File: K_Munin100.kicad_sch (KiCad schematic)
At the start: 95 parts, among them IC2 ACHS-7123-000E, J1 Conn_Coaxial, J19 To P.A., J2 Conn_Coaxial, J3 Conn_02x03_Odd_Even, J5 Wurth Redcube 7461057, J6 Phoenix/1711725, J7 Wurth Redcube 7461057, Q1 MRF101AN tab dwn, Q2 MRF 101BN tab up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

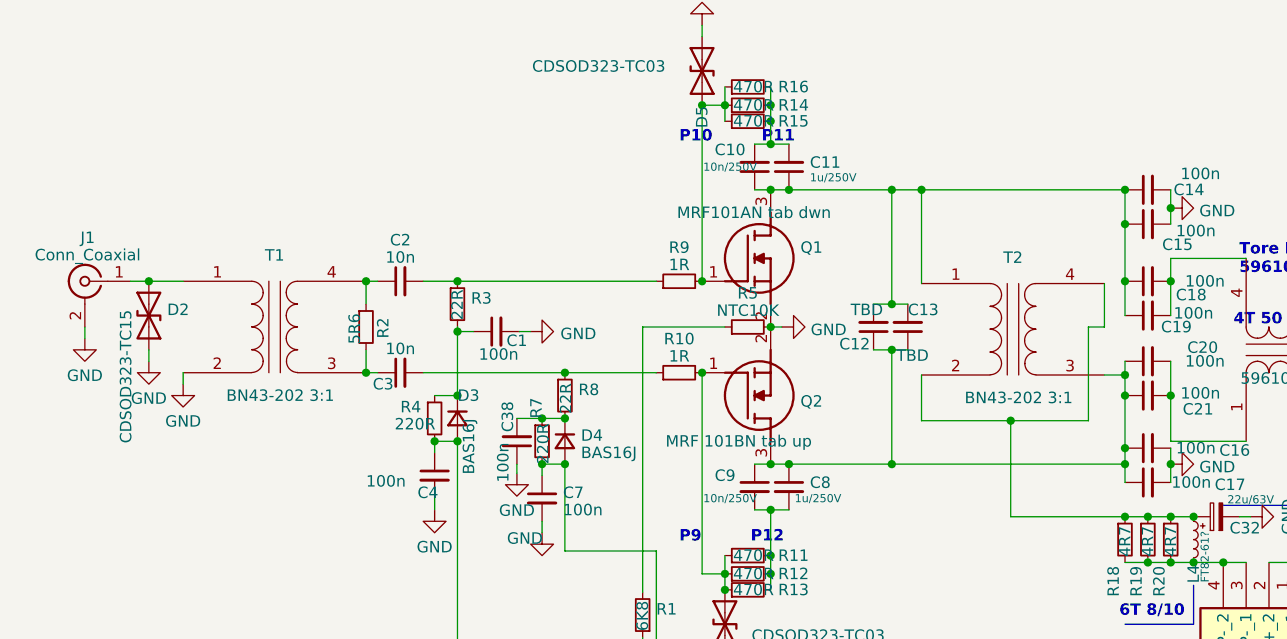
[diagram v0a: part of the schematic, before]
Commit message: Munin 400 mod with MRF101 AN/BN
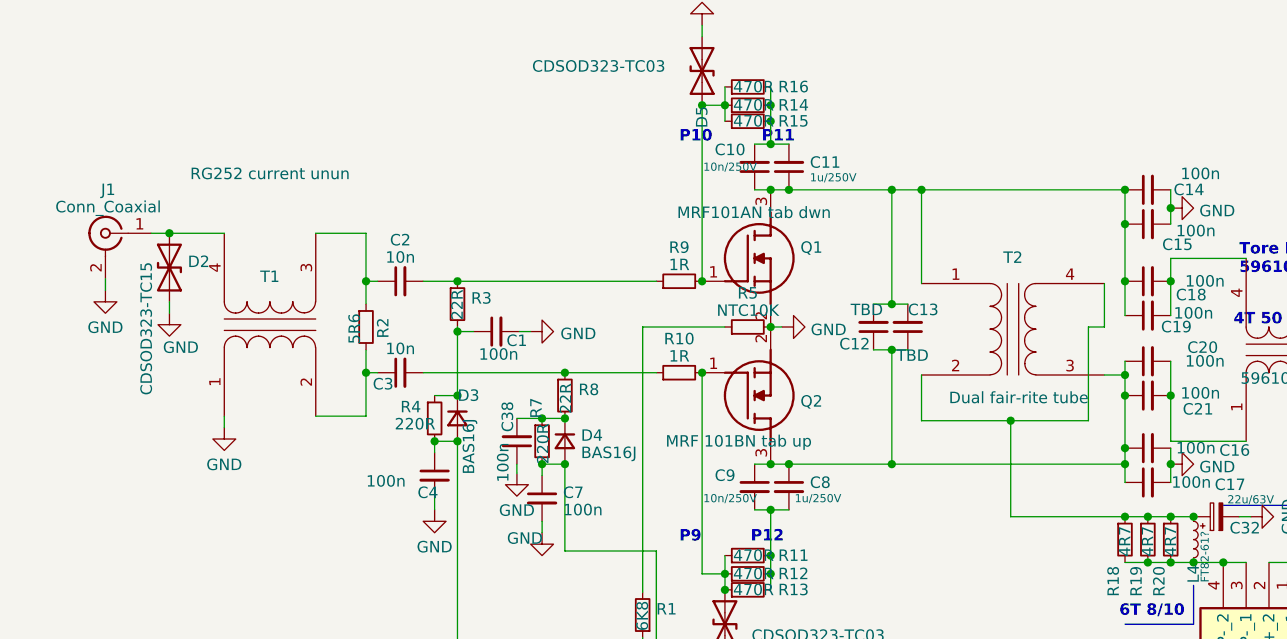
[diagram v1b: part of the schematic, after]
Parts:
- T1: value BN43-202 3:1 -> RG252 current unun
- T2: value BN43-202 3:1 -> Dual fair-rite tube
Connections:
- net GND: now also T1.1 (AA); no longer T1.2 (AB)
- net at D2.2 (A2), J1.1 (In): now also T1.4 (SB); no longer T1.1 (AA)
- net at C2.1, R2.1: now also T1.3 (SA); no longer T1.4 (SB)
- net at C3.1, R2.2: now also T1.2 (AB); no longer T1.3 (SA)
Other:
- moved on the sheet: D2, J1, T1
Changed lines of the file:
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@@
 	)
 	(junction
+		(at 64.008 56.134)
+		(diameter 0)
+		(color 0 0 0 0)
+	)
+	(junction
 		(at 108.966 76.454)
 		(diameter 0)
@@
 	)
 	(junction
-		(at 64.008 56.134)
-		(diameter 0)
-		(color 0 0 0 0)
-	)
-	(junction
 		(at 88.138 133.604)
 		(diameter 0)
@@
 	)
 	(junction
+		(at 64.008 45.974)
+		(diameter 0)
+		(color 0 0 0 0)
+	)
+	(junction
 		(at 86.106 56.134)
 		(diameter 0)
@@
 	)
 	(junction
-		(at 39.878 45.974)
+		(at 42.164 40.64)
 		(diameter 0)
 		(color 0 0 0 0)
@@
 	)
 	(junction
-		(at 64.008 45.974)
-		(diameter 0)
-		(color 0 0 0 0)
-	)
-	(junction
 		(at 148.336 58.674)
 		(diameter 0)
@@
 	(wire
 		(pts
+			(xy 58.42 60.96) (xy 64.008 60.96)
+		)
+		(stroke
+			(width 0)
+			(type default)
+		)
+	)
+	(wire
+		(pts
 			(xy 81.026 51.562) (xy 82.296 51.562)
 		)
@@
 	(wire
 		(pts
-			(xy 39.878 53.594) (xy 39.878 54.864)
+			(xy 42.164 48.26) (xy 42.164 49.53)
 		)
 		(stroke
@@
 	(wire
 		(pts
+			(xy 64.008 45.974) (xy 64.008 40.64)
+		)
+		(stroke
+			(width 0)
+			(type default)
+		)
+	)
+	(wire
+		(pts
 			(xy 122.428 66.294) (xy 148.336 66.294)
 		)
@@
 	(wire
 		(pts
-			(xy 39.878 45.974) (xy 43.688 45.974)
+			(xy 42.164 40.64) (xy 48.26 40.64)
 		)
 		(stroke
@@
 	(wire
 		(pts
-			(xy 37.846 45.974) (xy 39.878 45.974)
+			(xy 40.132 40.64) (xy 42.164 40.64)
 		)
 		(stroke
@@
 	(wire
 		(pts
+			(xy 64.008 40.64) (xy 58.42 40.64)
+		)
+		(stroke
+			(width 0)
+			(type default)
+		)
+	)
+	(wire
+		(pts
 			(xy 101.346 121.666) (xy 101.346 122.936)
 		)
@@
 	(wire
 		(pts
-			(xy 43.688 56.134) (xy 43.688 57.404)
+			(xy 48.26 60.96) (xy 48.26 62.23)
 		)
 		(stroke
@@
 	(wire
 		(pts
+			(xy 64.008 60.96) (xy 64.008 56.134)
+		)
+		(stroke
+			(width 0)
+			(type default)
+		)
+	)
+	(wire
+		(pts
 			(xy 165.608 136.906) (xy 165.608 133.096)
 		)
@@
 	(wire
 		(pts
-			(xy 32.766 51.054) (xy 32.766 52.324)
+			(xy 35.052 45.72) (xy 35.052 46.99)
 		)
 		(stroke
@@
 			)
 		)
-		(property "Value" "BN43-202  3:1"
+		(property "Value" "Dual fair-rite tube "
 			(at 136.525 58.928 0)
 			(effects
@@
 	(symbol
 		(lib_id "power:GND")
-		(at 43.688 57.404 0)
+		(at 48.26 62.23 0)
 		(unit 1)
 		(exclude_from_sim no)
@@
 		(fields_autoplaced yes)
 		(property "Reference" "#PWR07"
-			(at 43.688 63.754 0)
+			(at 48.26 68.58 0)
 			(effects
 				(font
@@
 		)
 		(property "Value" "GND"
-			(at 43.688 61.5395 0)
+			(at 48.26 66.3655 0)
 			(effects
 				(font
@@
 		)
 		(property "Footprint" ""
-			(at 43.688 57.404 0)
+			(at 48.26 62.23 0)
 			(effects
 				(font
@@
 		)
 		(property "Datasheet" ""
-			(at 43.688 57.404 0)
+			(at 48.26 62.23 0)
 			(effects
 				(font
@@
 		)
 		(property "Description" ""
-			(at 43.688 57.404 0)
+			(at 48.26 62.23 0)
 			(effects
 				(font
@@
 	(symbol
 		(lib_id "Diode:1N62xxCA")
-		(at 39.878 49.784 90)
+		(at 42.164 44.45 90)
 		(unit 1)
 		(exclude_from_sim no)
@@
 		(dnp no)
 		(property "Reference" "D2"
-			(at 41.91 49.1403 90)
+			(at 44.196 43.8063 90)
 			(effects
 				(font
@@
 		)
 		(property "Value" "CDSOD323-TC15"
-			(at 37.338 49.149 0)
+			(at 39.624 43.815 0)
 			(effects
 				(font
@@
 		)
 		(property "Footprint" "Diode_SMD:D_SOD-323_HandSoldering"
-			(at 44.958 49.784 0)
+			(at 47.244 44.45 0)
 			(effects
 				(font
@@
 		)
 		(property "Datasheet" "https://www.vishay.com/docs/88301/15ke.pdf"
-			(at 39.878 49.784 0)
+			(at 42.164 44.45 0)
 			(effects
 				(font
@@
 		)
 		(property "Description" ""
-			(at 39.878 49.784 0)
+			(at 42.164 44.45 0)
 			(effects
 				(font
@@
 	(symbol
 		(lib_id "Device:Transformer_1P_1S")
-		(at 53.848 51.054 0)
+		(at 53.34 50.8 90)
 		(unit 1)
 		(exclude_from_sim no)
@@
 		(dnp no)
 		(property "Reference" "T1"
-			(at 53.8607 43.0909 0)
+			(at 53.34 45.466 90)
 			(effects
 				(font
@@
 			)
 		)
-		(property "Value" "BN43-202  3:1"
-			(at 54.483 58.674 0)
+		(property "Value" "RG252 current unun"
+			(at 53.34 34.036 90)
 			(effects
 				(font
@@
 		)
 		(property "Footprint" "BN43-202-master:BN43-202"
-			(at 53.848 51.054 0)
+			(at 53.34 50.8 0)
 			(effects
 				(font
@@
 		)
 		(property "Datasheet" "~"
-			(at 53.848 51.054 0)
+			(at 53.34 50.8 0)
 			(effects
 				(font
@@
 		)
 		(property "Description" ""
-			(at 53.848 51.054 0)
+			(at 53.34 50.8 0)
 			(effects
 				(font
@@
 	(symbol
 		(lib_id "power:GND")
-		(at 32.766 52.324 0)
+		(at 35.052 46.99 0)
 		(unit 1)
 		(exclude_from_sim no)
@@
 		(fields_autoplaced yes)
 		(property "Reference" "#PWR01"
-			(at 32.766 58.674 0)
+			(at 35.052 53.34 0)
 			(effects
 				(font
@@
 		)
 		(property "Value" "GND"
-			(at 32.766 56.4595 0)
+			(at 35.052 51.1255 0)
 			(effects
 				(font
@@
 		)
 		(property "Footprint" ""
-			(at 32.766 52.324 0)
+			(at 35.052 46.99 0)
 			(effects
 				(font
@@
 		)
 		(property "Datasheet" ""
-			(at 32.766 52.324 0)
+			(at 35.052 46.99 0)
 			(effects
 				(font
@@
 		)
 		(property "Description" ""
-			(at 32.766 52.324 0)
+			(at 35.052 46.99 0)
 			(effects
 				(font
@@
 	(symbol
 		(lib_id "Connector:Conn_Coaxial")
-		(at 32.766 45.974 0)
+		(at 35.052 40.64 0)
 		(mirror y)
 		(unit 1)
@@
 		(fields_autoplaced yes)
 		(property "Reference" "J1"
-			(at 33.0834 41.1375 0)
+			(at 35.3694 35.8035 0)
 			(effects
 				(font
@@
 		)
 		(property "Value" "Conn_Coaxial"
-			(at 33.0834 43.0585 0)
+			(at 35.3694 37.7245 0)
 			(effects
 				(font
@@
 		)
 		(property "Footprint" "SMA_PINS:SMA_PINS"
-			(at 32.766 45.974 0)
+			(at 35.052 40.64 0)
 			(effects
 				(font
@@
 		)
 		(property "Datasheet" " ~"
-			(at 32.766 45.974 0)
+			(at 35.052 40.64 0)
 			(effects
 				(font
@@
 		)
 		(property "Description" ""
-			(at 32.766 45.974 0)
+			(at 35.052 40.64 0)
 			(effects
 				(font
@@
 	(symbol
 		(lib_id "power:GND")
-		(at 39.878 54.864 0)
+		(at 42.164 49.53 0)
 		(unit 1)
 		(exclude_from_sim no)
@@
 		(on_board yes)
 		(dnp no)
-		(fields_autoplaced yes)
 		(property "Reference" "#PWR08"
-			(at 39.878 61.214 0)
+			(at 42.164 55.88 0)
 			(effects
 				(font
@@
 		)
 		(property "Value" "GND"
-			(at 39.878 58.9995 0)
+			(at 43.434 53.34 0)
 			(effects
 				(font
@@
 		)
 		(property "Footprint" ""
-			(at 39.878 54.864 0)
+			(at 42.164 49.53 0)
 			(effects
 				(font
@@
 		)
 		(property "Datasheet" ""
-			(at 39.878 54.864 0)
+			(at 42.164 49.53 0)
 			(effects
 				(font
@@
 		)
 		(property "Description" ""
-			(at 39.878 54.864 0)
+			(at 42.164 49.53 0)
 			(effects
 				(font
